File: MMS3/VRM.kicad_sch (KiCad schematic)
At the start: 37 parts, among them U15 AMS1117-3.3, U3 TPS54560BDDA

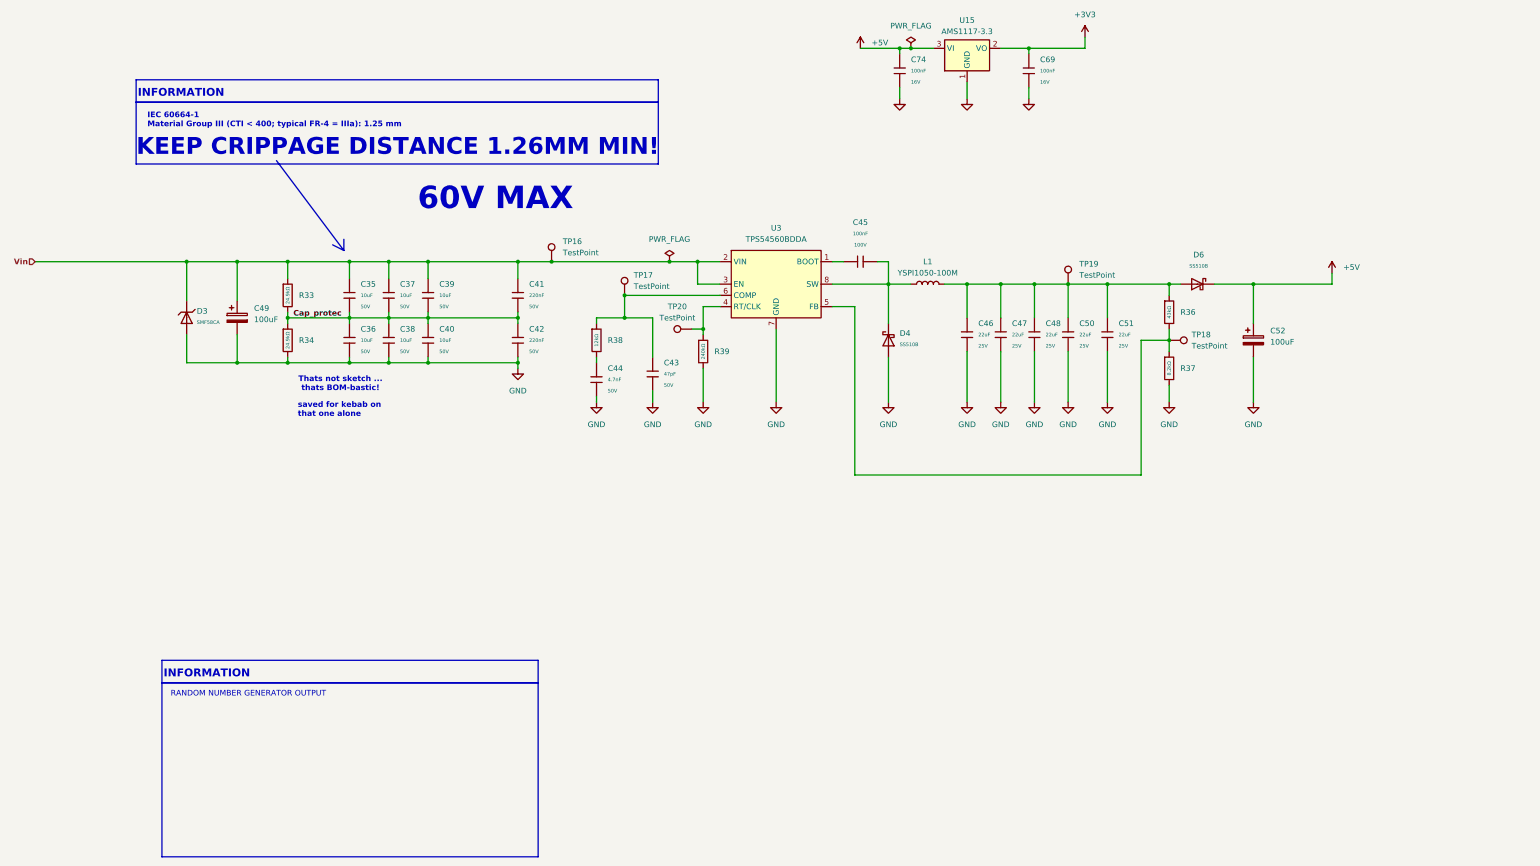
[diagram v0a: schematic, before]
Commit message: updated schematic, removed annotation
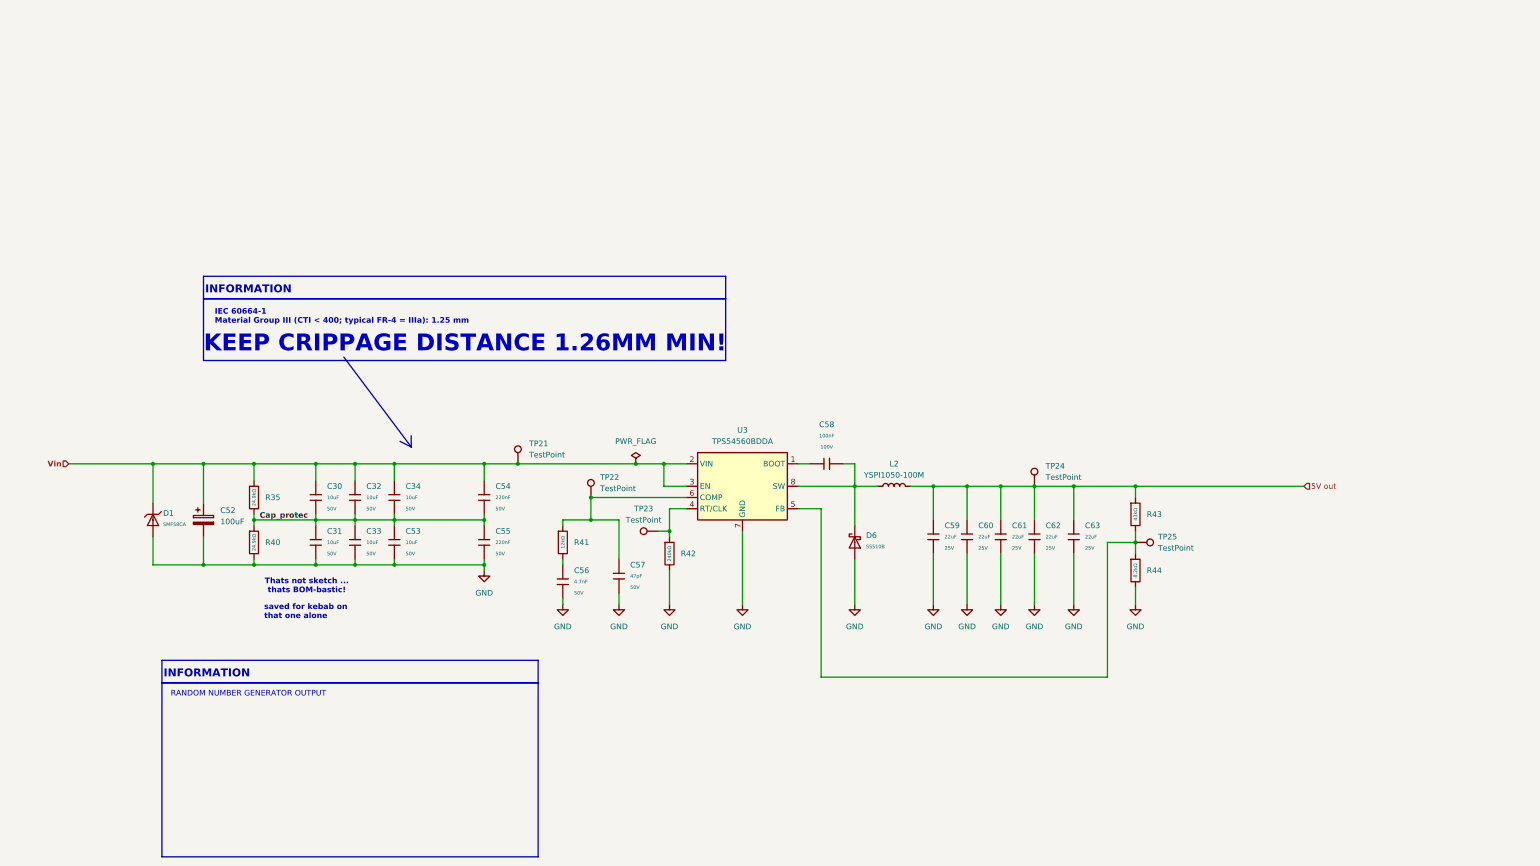
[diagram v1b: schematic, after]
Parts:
- removed C35, C36, C37, C38, C39, C40: 10uF, PCM_JLCPCB:C_0805, symbol PCM_JLCPCB-Capacitors:0805,10uF,(2)
- removed C41, C42: 220nF, PCM_JLCPCB:C_0805, symbol PCM_JLCPCB-Capacitors:0805,220nF
- removed C43: 47pF, PCM_JLCPCB:C_0402, symbol PCM_JLCPCB-Capacitors:0402,47pF
- removed C44: 4.7nF, PCM_JLCPCB:C_0402, symbol PCM_JLCPCB-Capacitors:0402,4.7nF
- removed C45: 100nF, PCM_JLCPCB:C_0805, symbol PCM_JLCPCB-Capacitors:0805,100nF
- removed C46, C47, C48, C50, C51: 22uF, PCM_JLCPCB:C_0805, symbol PCM_JLCPCB-Capacitors:0805,22uF
- removed C49: 100uF, Capacitor_SMD:CP_Elec_10x10, symbol Device:C_Polarized
- removed C69, C74: 100nF, PCM_JLCPCB:C_0402, symbol PCM_JLCPCB-Capacitors:0402,100nF
- removed D3: SMF58CA, PCM_JLCPCB:D_SOD-123FL, symbol PCM_JLCPCB-Diodes:TVS-Uni,SMF58CA
- removed D4: SS510B, PCM_JLCPCB:D_SMB, symbol PCM_JLCPCB-Diodes:Schottky,SS510B
- removed L1: YSPI1050-100M, Inductor_SMD:L_Sunlord_MWSA1005S, symbol Device:L
- removed R33, R34: 24.9kΩ, PCM_JLCPCB:R_0402, symbol PCM_JLCPCB-Resistors:0402,24kΩ
- removed R36: 43kΩ, PCM_JLCPCB:R_0603, symbol PCM_JLCPCB-Resistors:0603,43kΩ
- removed R37: 8.2kΩ, PCM_JLCPCB:R_0402, symbol PCM_JLCPCB-Resistors:0402,8.2kΩ
- removed R38: 12kΩ, PCM_JLCPCB:R_0402, symbol PCM_JLCPCB-Resistors:0402,12kΩ
- removed R39: 240kΩ, PCM_JLCPCB:R_0603, symbol PCM_JLCPCB-Resistors:0603,240kΩ
- removed TP16, TP17, TP18, TP19, TP20: TestPoint, TestPoint:TestPoint_Pad_D1.0mm, symbol Connector:TestPoint
- removed U15: AMS1117-3.3, Package_TO_SOT_SMD:SOT-223-3_TabPin2, symbol Regulator_Linear:AMS1117-3.3
- added C30, C31, C32, C33, C34, C53: 10uF, PCM_JLCPCB:C_0805, symbol PCM_JLCPCB-Capacitors:0805,10uF,(2)
- added C54, C55: 220nF, PCM_JLCPCB:C_0805, symbol PCM_JLCPCB-Capacitors:0805,220nF
- added C56: 4.7nF, PCM_JLCPCB:C_0402, symbol PCM_JLCPCB-Capacitors:0402,4.7nF
- added C57: 47pF, PCM_JLCPCB:C_0402, symbol PCM_JLCPCB-Capacitors:0402,47pF
- added C58: 100nF, PCM_JLCPCB:C_0805, symbol PCM_JLCPCB-Capacitors:0805,100nF
- added C59, C60, C61, C62, C63: 22uF, PCM_JLCPCB:C_0805, symbol PCM_JLCPCB-Capacitors:0805,22uF
- added D1: SMF58CA, PCM_JLCPCB:D_SOD-123FL, symbol PCM_JLCPCB-Diodes:TVS-Uni,SMF58CA
- added L2: YSPI1050-100M, Inductor_SMD:L_Sunlord_MWSA1005S, symbol Device:L
- added R35, R40: 24.9kΩ, PCM_JLCPCB:R_0402, symbol PCM_JLCPCB-Resistors:0402,24kΩ
- added R41: 12kΩ, PCM_JLCPCB:R_0402, symbol PCM_JLCPCB-Resistors:0402,12kΩ
- added R42: 240kΩ, PCM_JLCPCB:R_0603, symbol PCM_JLCPCB-Resistors:0603,240kΩ
- added R43: 43kΩ, PCM_JLCPCB:R_0603, symbol PCM_JLCPCB-Resistors:0603,43kΩ
- added R44: 8.2kΩ, PCM_JLCPCB:R_0402, symbol PCM_JLCPCB-Resistors:0402,8.2kΩ
- added TP21, TP22, TP23, TP24, TP25: TestPoint, TestPoint:TestPoint_Pad_D1.0mm, symbol Connector:TestPoint
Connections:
- net Cap_protec: now also C30.2, C31.1, C32.2, C33.1, C34.2, C53.1, C54.2, C55.1, R35.2, R40.1
- net GND: now also D6.2, C31.2, C33.2, C53.2, C55.2, C56.2, C57.2, C59.2, C60.2, C61.2, C62.2, C63.2, D1.2, R40.2, R42.2, R44.2
- net Vin: now also C52.1, C30.1, C32.1, C34.1, C54.1, D1.1, R35.1, TP21.1
- net at U3.6 (COMP): now also C57.1, R41.1, TP22.1
- net at U3.4 (RT/CLK): now also R42.1, TP23.1
- net at U3.5 (FB): now also R43.2, R44.1, TP25.1
- net at U3.8 (SW): now also D6.1, C58.1, L2.1
- net at U3.1 (BOOT): now also C58.2
- removed net +5V: C52.1, D6.1
- new net: C56.1, R41.2
- new net 5V out: C59.1, C60.1, C61.1, C62.1, C63.1, L2.2, R43.1, TP24.1
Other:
- note removed: "60V MAX"
- title: MMS3 -> MMS3 CH32L103 Version

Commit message: initial PCB update
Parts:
- removed C30, C31, C32, C33, C34, C53: 10uF, PCM_JLCPCB:C_0805, symbol PCM_JLCPCB-Capacitors:0805,10uF,(2)
- removed C52: 100uF, Capacitor_SMD:CP_Elec_10x10, symbol Device:C_Polarized
- removed C54, C55: 220nF, PCM_JLCPCB:C_0805, symbol PCM_JLCPCB-Capacitors:0805,220nF
- removed C56: 4.7nF, PCM_JLCPCB:C_0402, symbol PCM_JLCPCB-Capacitors:0402,4.7nF
- removed C57: 47pF, PCM_JLCPCB:C_0402, symbol PCM_JLCPCB-Capacitors:0402,47pF
- removed C58: 100nF, PCM_JLCPCB:C_0805, symbol PCM_JLCPCB-Capacitors:0805,100nF
- removed C59, C60, C61, C62, C63: 22uF, PCM_JLCPCB:C_0805, symbol PCM_JLCPCB-Capacitors:0805,22uF
- removed D1: SMF58CA, PCM_JLCPCB:D_SOD-123FL, symbol PCM_JLCPCB-Diodes:TVS-Uni,SMF58CA
- removed D6: SS510B, PCM_JLCPCB:D_SMB, symbol PCM_JLCPCB-Diodes:Schottky,SS510B
- removed L2: YSPI1050-100M, Inductor_SMD:L_Sunlord_MWSA1005S, symbol Device:L
- removed R35, R40: 24.9kΩ, PCM_JLCPCB:R_0402, symbol PCM_JLCPCB-Resistors:0402,24kΩ
- removed R41: 12kΩ, PCM_JLCPCB:R_0402, symbol PCM_JLCPCB-Resistors:0402,12kΩ
- removed R42: 240kΩ, PCM_JLCPCB:R_0603, symbol PCM_JLCPCB-Resistors:0603,240kΩ
- removed R43: 43kΩ, PCM_JLCPCB:R_0603, symbol PCM_JLCPCB-Resistors:0603,43kΩ
- removed R44: 8.2kΩ, PCM_JLCPCB:R_0402, symbol PCM_JLCPCB-Resistors:0402,8.2kΩ
- removed TP21, TP22, TP23, TP24, TP25: TestPoint, TestPoint:TestPoint_Pad_D1.0mm, symbol Connector:TestPoint
- removed U3: TPS54560BDDA, Package_SO:Texas_R-PDSO-G8_EP2.95x4.9mm_Mask2.4x3.1mm_ThermalVias, symbol Regulator_Switching:TPS54560BDDA
- added C35, C36, C37, C38, C39, C40: 10uF, PCM_JLCPCB:C_0805, symbol PCM_JLCPCB-Capacitors:0805,10uF,(2)
- added C41, C42: 220nF, PCM_JLCPCB:C_0805, symbol PCM_JLCPCB-Capacitors:0805,220nF
- added C43: 47pF, PCM_JLCPCB:C_0402, symbol PCM_JLCPCB-Capacitors:0402,47pF
- added C44: 4.7nF, PCM_JLCPCB:C_0402, symbol PCM_JLCPCB-Capacitors:0402,4.7nF
- added C45: 100nF, PCM_JLCPCB:C_0805, symbol PCM_JLCPCB-Capacitors:0805,100nF
- added C46, C47, C48, C50, C51: 22uF, PCM_JLCPCB:C_0805, symbol PCM_JLCPCB-Capacitors:0805,22uF
- added C49: 100uF, Capacitor_SMD:CP_Elec_10x10, symbol Device:C_Polarized
- added D2: SMF58CA, PCM_JLCPCB:D_SOD-123FL, symbol PCM_JLCPCB-Diodes:TVS-Uni,SMF58CA
- added D3: SS510B, PCM_JLCPCB:D_SMB, symbol PCM_JLCPCB-Diodes:Schottky,SS510B
- added L1: YSPI1050-100M, Inductor_SMD:L_Sunlord_MWSA1005S, symbol Device:L
- added R33, R34: 24.9kΩ, PCM_JLCPCB:R_0402, symbol PCM_JLCPCB-Resistors:0402,24kΩ
- added R36: 43kΩ, PCM_JLCPCB:R_0603, symbol PCM_JLCPCB-Resistors:0603,43kΩ
- added R37: 8.2kΩ, PCM_JLCPCB:R_0402, symbol PCM_JLCPCB-Resistors:0402,8.2kΩ
- added R38: 12kΩ, PCM_JLCPCB:R_0402, symbol PCM_JLCPCB-Resistors:0402,12kΩ
- added R39: 240kΩ, PCM_JLCPCB:R_0603, symbol PCM_JLCPCB-Resistors:0603,240kΩ
- added TP16, TP17, TP18, TP19, TP20: TestPoint, TestPoint:TestPoint_Pad_D1.0mm, symbol Connector:TestPoint
- added U2: TPS54560BDDA, Package_SO:Texas_R-PDSO-G8_EP2.95x4.9mm_Mask2.4x3.1mm_ThermalVias, symbol Regulator_Switching:TPS54560BDDA
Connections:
- net 5V out: now also C46.1, C47.1, C48.1, C50.1, C51.1, L1.2, R36.1, TP19.1
- net Cap_protec: now also C35.2, C36.1, C37.2, C38.1, C39.2, C40.1, C41.2, C42.1, R33.2, R34.1
- net GND: now also C36.2, C38.2, C40.2, C42.2, C43.2, C44.2, C46.2, C47.2, C48.2, C49.2, C50.2, C51.2, D2.2, D3.2, R34.2, R37.2, R39.2, U2.7 (GND), U2.9 (GND)
- net Vin: now also C35.1, C37.1, C39.1, C41.1, C49.1, D2.1, R33.1, TP16.1, U2.2 (VIN), U2.3 (EN)
- new net: C45.1, D3.1, L1.1, U2.8 (SW)
- new net: C45.2, U2.1 (BOOT)
- new net: C44.1, R38.2
- new net: C43.1, R38.1, TP17.1, U2.6 (COMP)
- new net: R39.1, TP20.1, U2.4 (RT/CLK)
- new net: R36.2, R37.1, TP18.1, U2.5 (FB)
